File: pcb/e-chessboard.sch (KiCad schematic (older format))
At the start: 55 parts

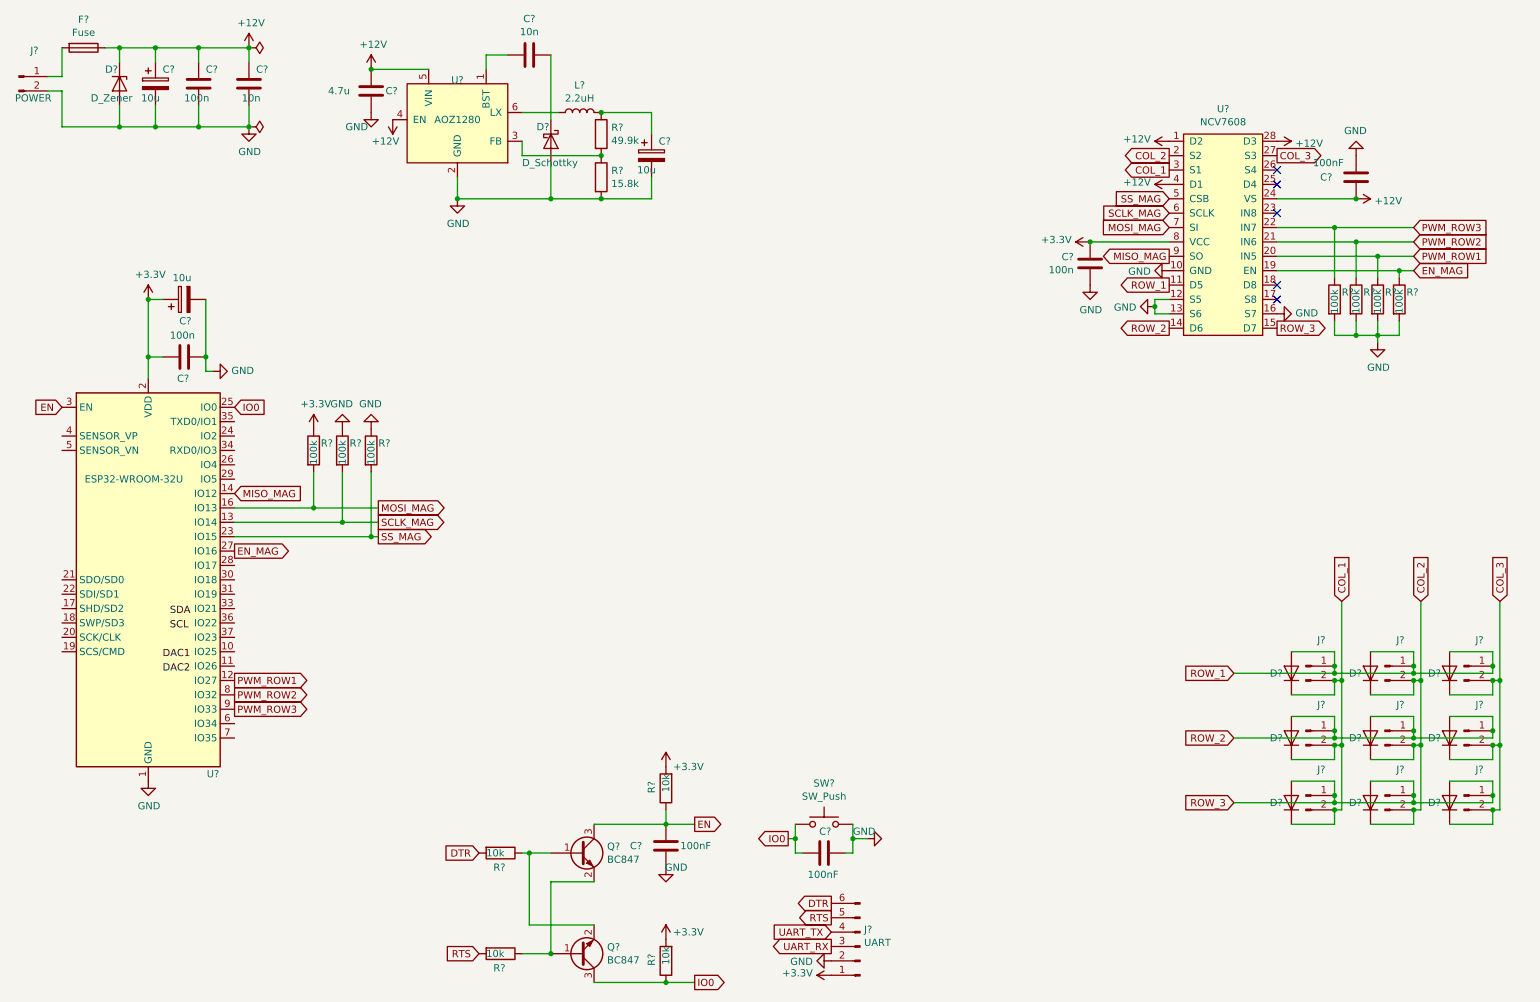
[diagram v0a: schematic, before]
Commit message: feat(kicad): Tidy up schematic
Adding blueboxes to schematic parts.
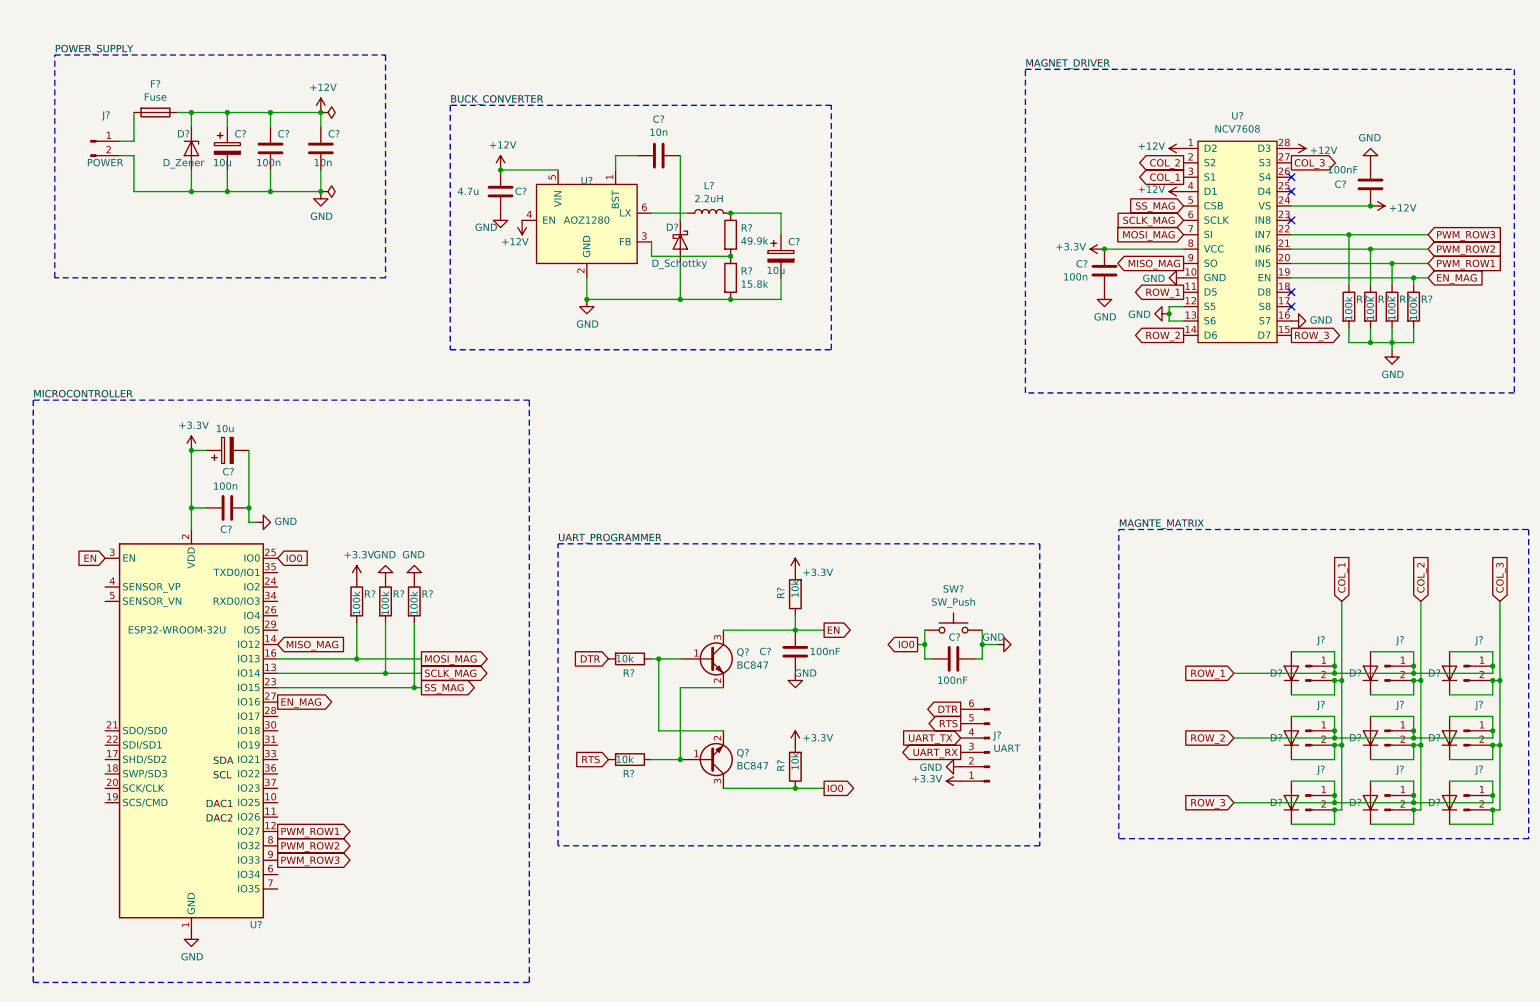
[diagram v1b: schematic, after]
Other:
- moved on the sheet: C?, D?, F?, J?, L?, Q?, R?, SW?, U?

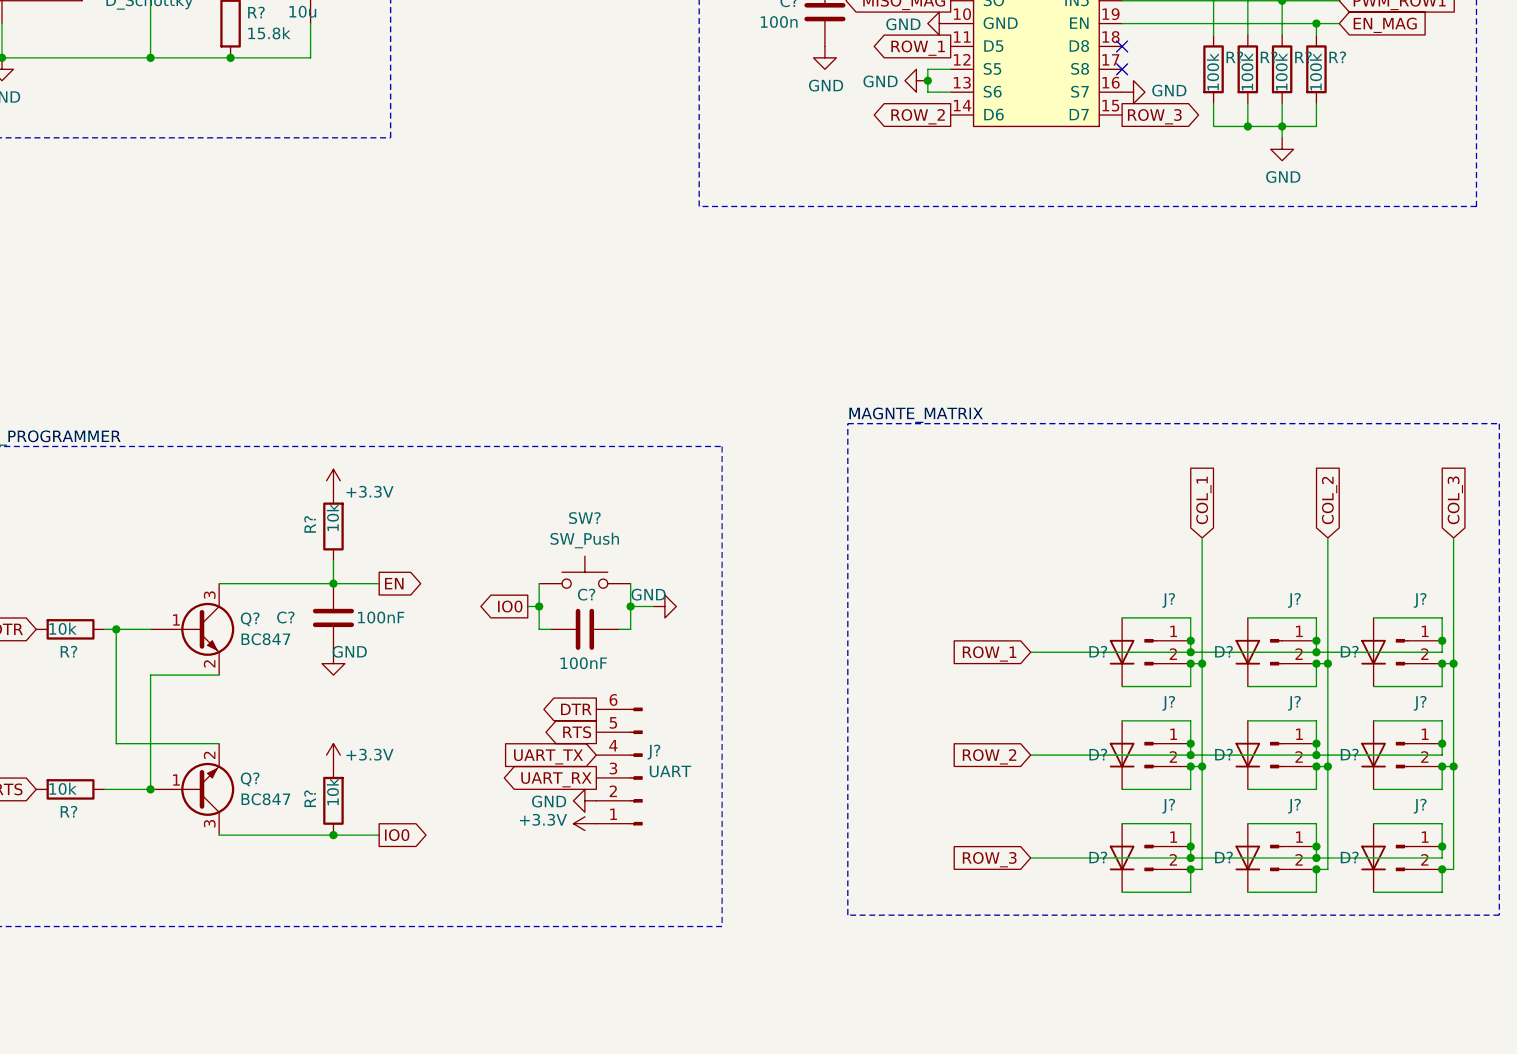
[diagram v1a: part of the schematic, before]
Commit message: feat(kicad): Adding mounting holes
Adding four M3 mounting holes.
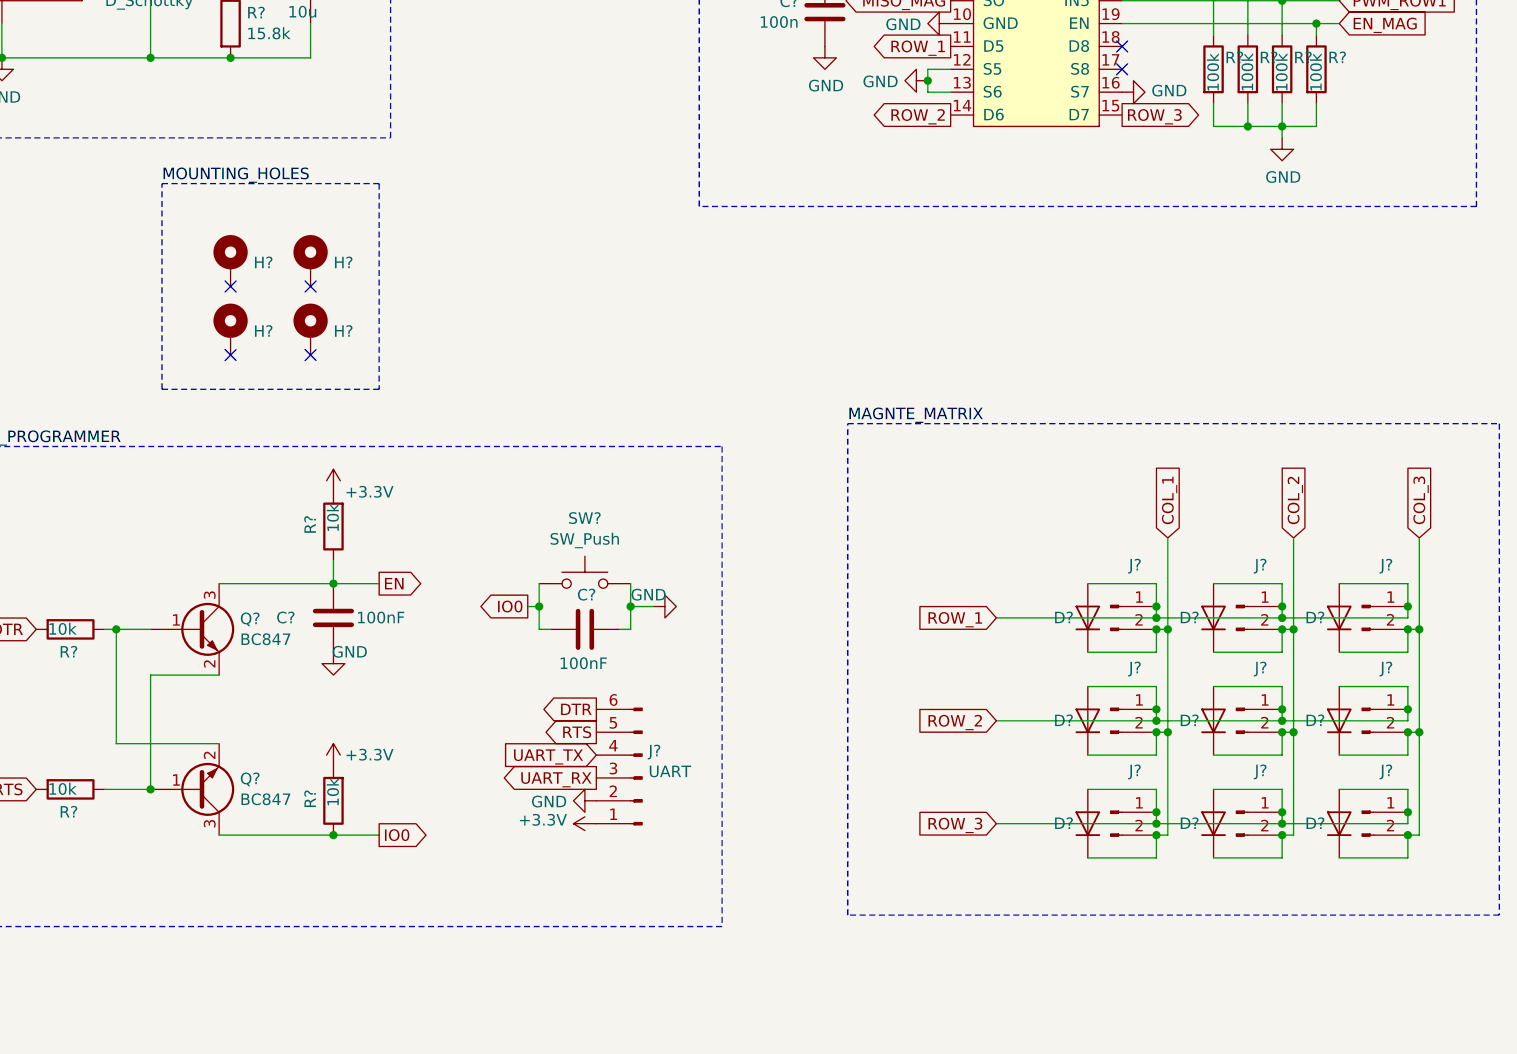
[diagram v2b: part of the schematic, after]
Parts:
- added H? (x4): MountingHole_Pad, MountingHole:MountingHole_3.2mm_M3_ISO7380_Pad, symbol Mechanical:MountingHole_Pad
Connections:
- no-connect marks 5 -> 9
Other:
- moved on the sheet: D?, J?

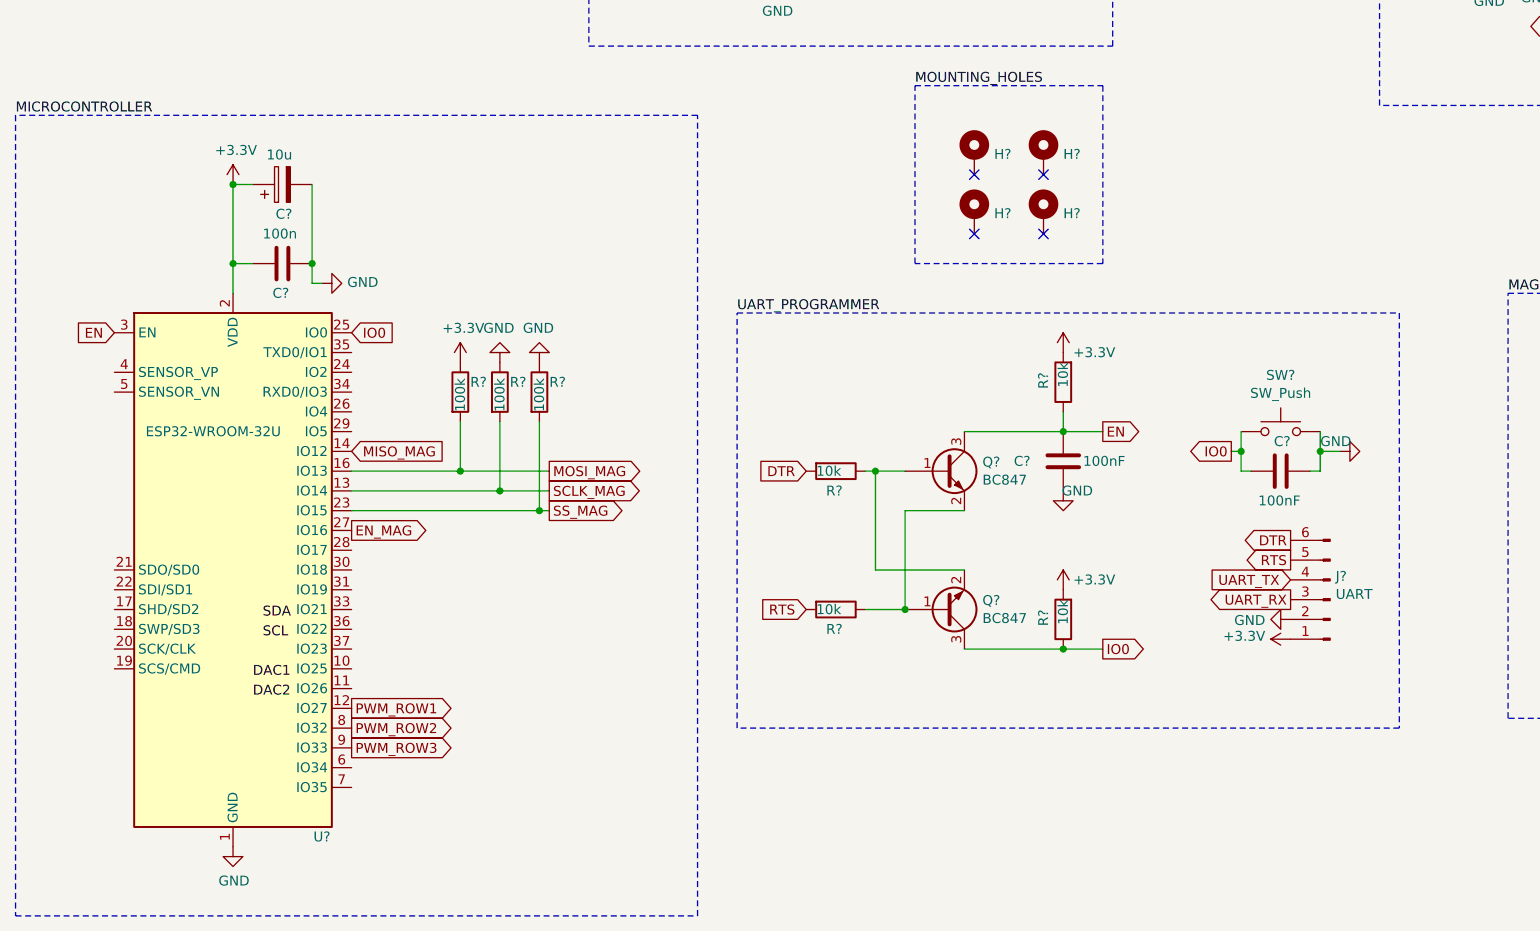
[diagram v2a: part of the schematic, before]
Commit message: fix(kicad): removing pull-up/down resistors
Removing pull-up/down resistors for spi and pwm. I'm using the build in
ones for simplification.
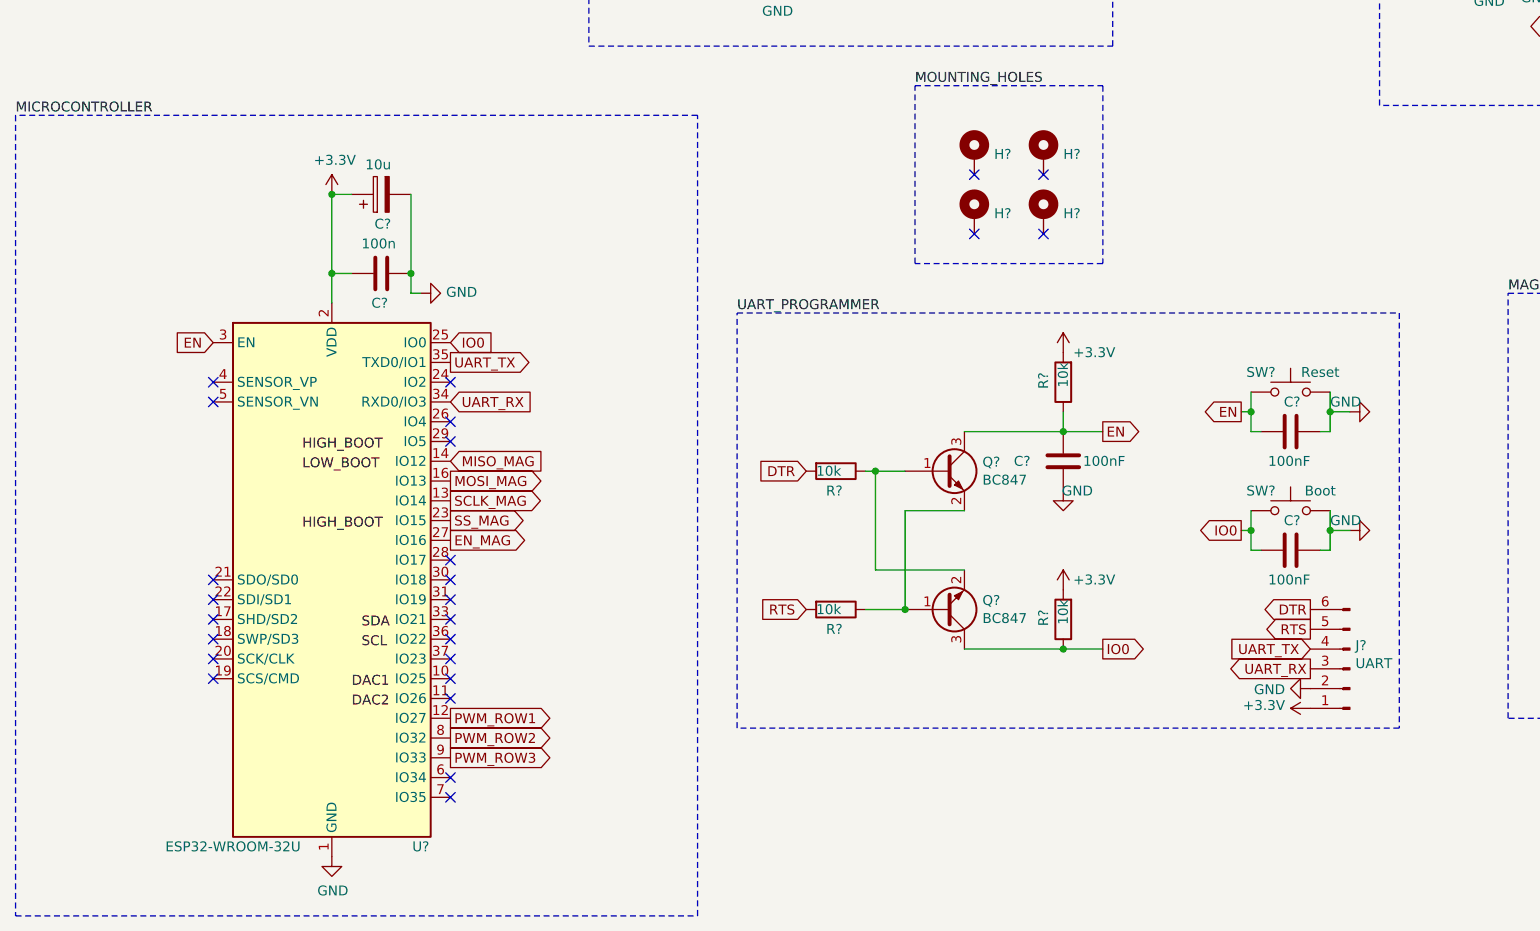
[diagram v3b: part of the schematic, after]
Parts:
- removed R? (x3): 100k, Resistor_SMD:R_0805_2012Metric, symbol Device:R
- added C?: 100nF, Capacitor_SMD:C_0805_2012Metric_Pad1.15x1.40mm_HandSolder, symbol Device:C
- added SW?: Reset, Button_Switch_SMD:SW_SPST_EVQPE1, symbol Switch:SW_Push
- SW?: value SW_Push -> Boot
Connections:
- net EN: now also C?.2, SW?.1
- net GND: now also C?.1, SW?.2
- net UART_RX: now also U?.34 (RXD0/IO3)
- net UART_TX: now also U?.35 (TXD0/IO1)
- no-connect marks 9 -> 30
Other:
- moved on the sheet: C?, J?, SW?, U?
